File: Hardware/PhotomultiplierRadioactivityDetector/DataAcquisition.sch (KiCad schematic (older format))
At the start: 27 parts, among them Q1 2N7002, Q2 Q_NJFET_DGS, Q7 Q_NJFET_DGS, U1 TL074, U3 TL074

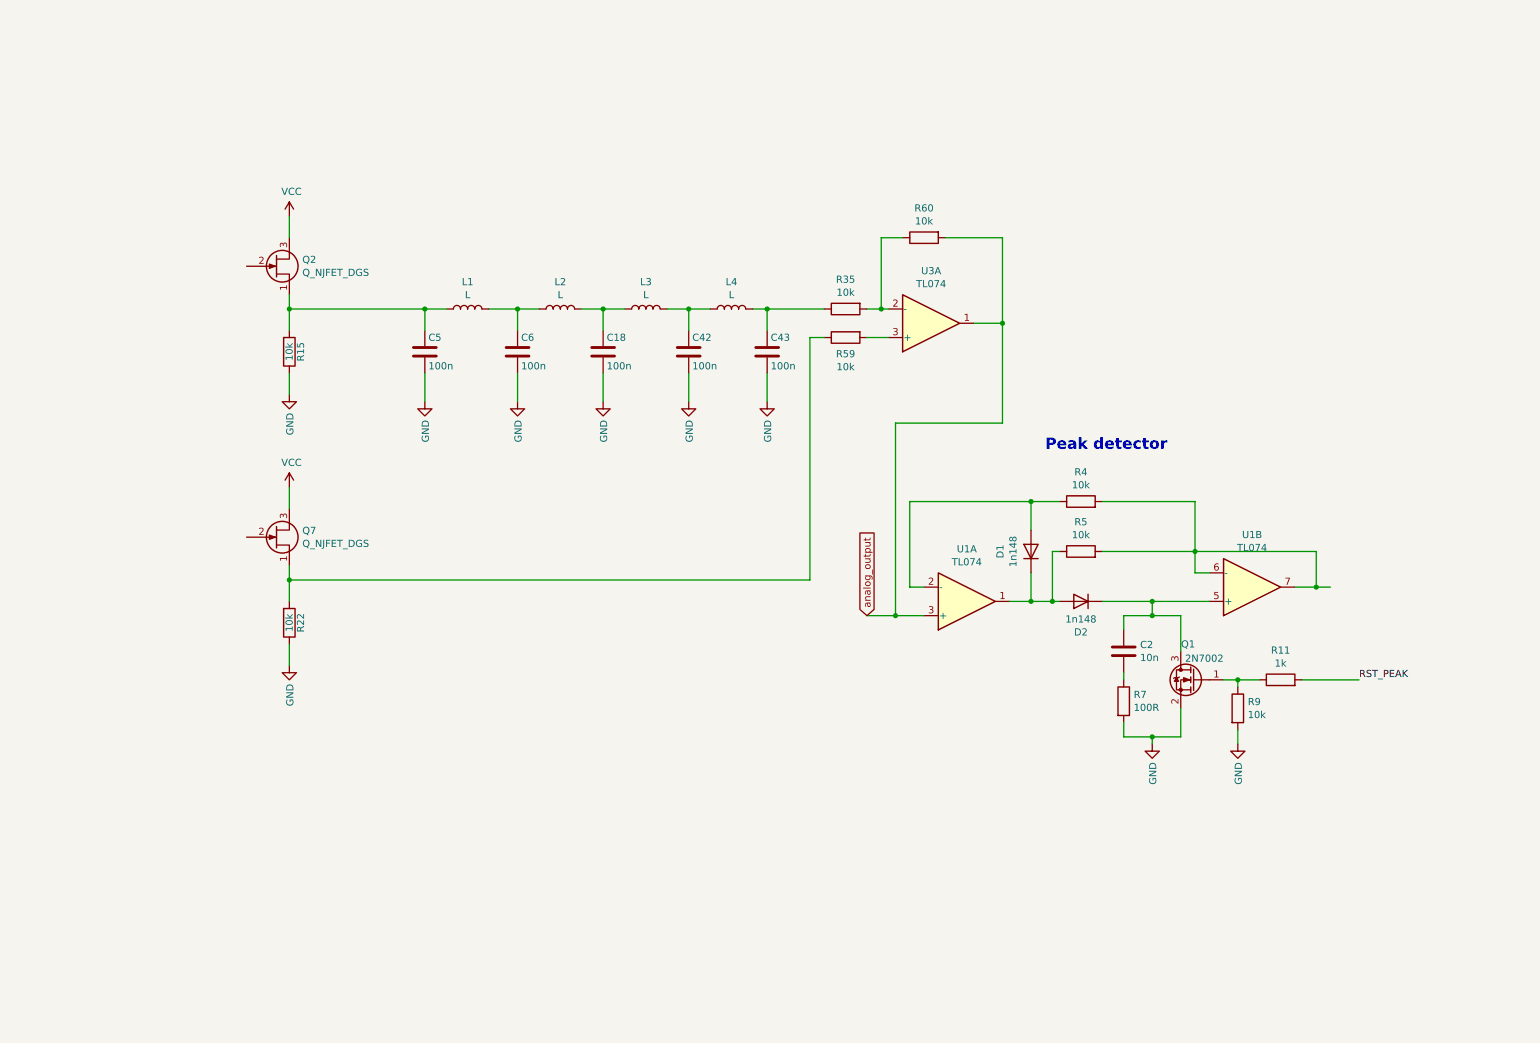
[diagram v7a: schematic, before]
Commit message: align to ltspice simulation
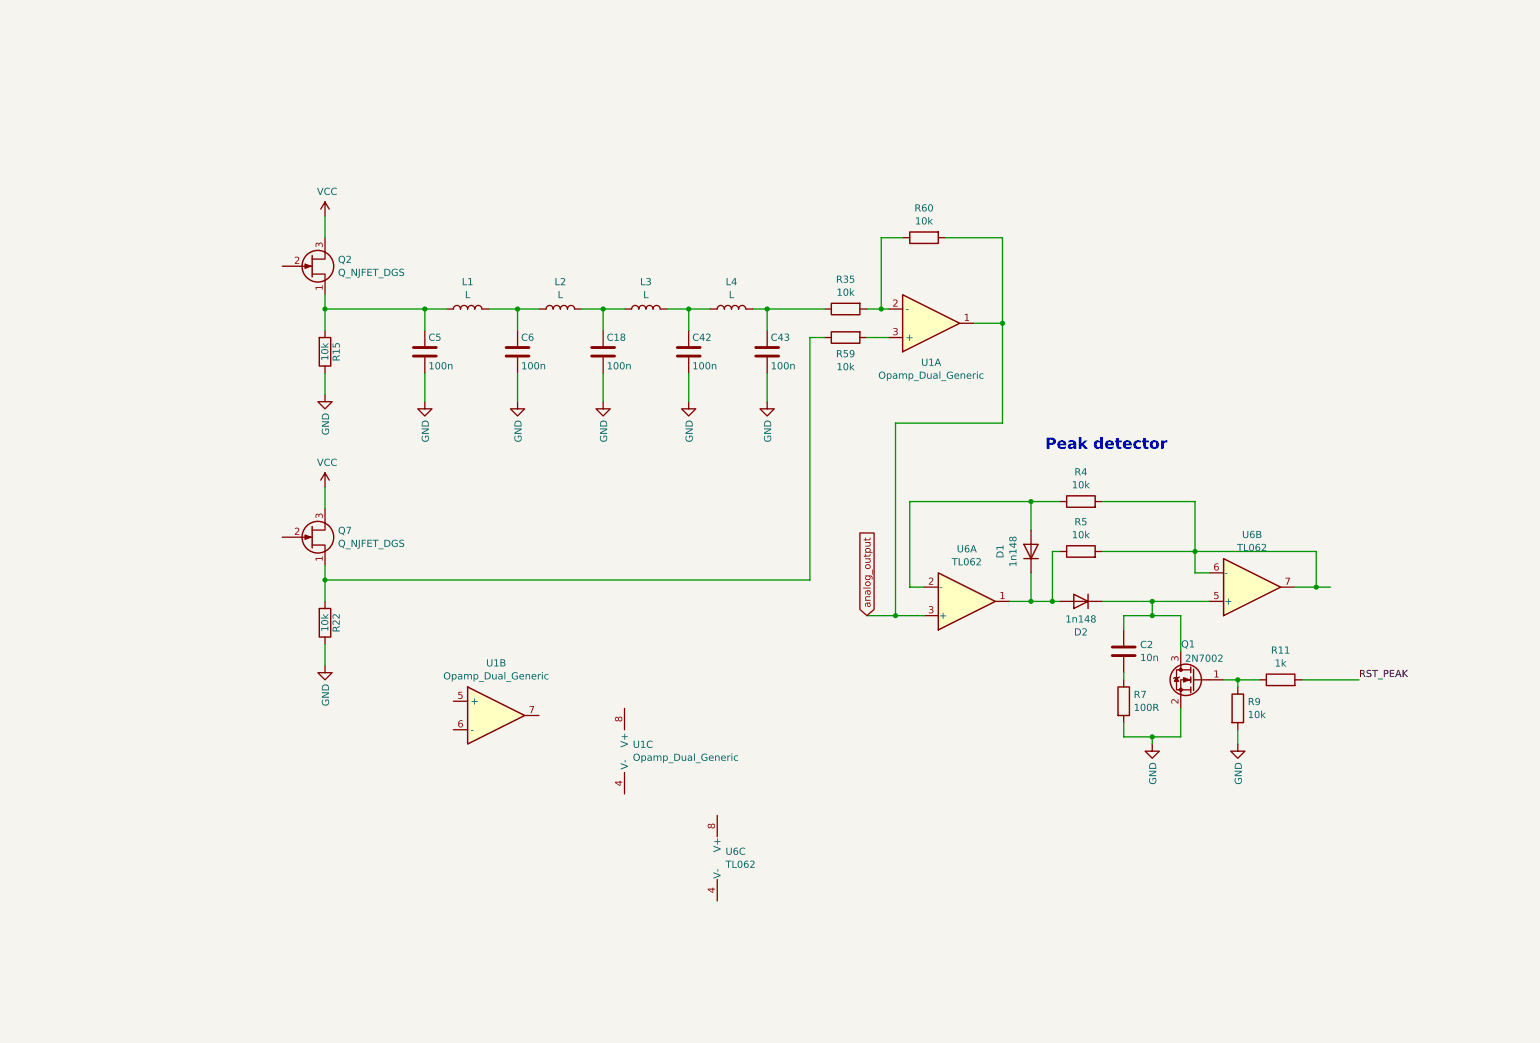
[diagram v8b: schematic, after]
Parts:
- removed U1, U3: TL074, Package_SO:SOIC-14_3.9x8.7mm_P1.27mm, symbol Amplifier_Operational:TL074
- added U1: Opamp_Dual_Generic, Package_SO:MSOP-8-1EP_3x3mm_P0.65mm_EP1.68x1.88mm, symbol Device:Opamp_Dual_Generic
- added U6: TL062, Package_SO:SO-8_5.3x6.2mm_P1.27mm, symbol Amplifier_Operational:TL062
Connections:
- net analog_output: now also U1.1, U6.3 (+)
- net at D1.1 (K), D2.2 (A), R5.1: now also U6.1
- net at D1.2 (A), R4.1: now also U6.2 (-)
- net at C2.2, D2.1 (K), Q1.3 (D): now also U6.5 (+)
- net at R4.2, R5.2: now also U6.6 (-), U6.7
- net at R35.2, R60.1: now also U1.2 (-)
- net at R59.2: now also U1.3 (+)
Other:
- moved on the sheet: Q2, Q7, R15, R22
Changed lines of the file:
@@
 Wire Wire Line
 	9200 5250 9350 5250
-$Comp
-L Amplifier_Operational:TL074 U1
-U 1 1 5ED99C75
-P 7300 4700
-F 0 "U1" H 7300 4333 50  0000 C CNN
-F 1 "TL074" H 7300 4424 50  0000 C CNN
-F 2 "Package_SO:SOIC-14_3.9x8.7mm_P1.27mm" H 7250 4800 50  0001 C CNN
-F 3 "http://www.ti.com/lit/ds/symlink/tl071.pdf" H 7350 4900 50  0001 C CNN
-	1    7300 4700
-	1    0    0    1
-$EndComp
-$Comp
-L Amplifier_Operational:TL074 U1
-U 2 1 5ED9B4E9
-P 9300 4600
-F 0 "U1" H 9300 4233 50  0000 C CNN
-F 1 "TL074" H 9300 4324 50  0000 C CNN
-F 2 "Package_SO:SOIC-14_3.9x8.7mm_P1.27mm" H 9250 4700 50  0001 C CNN
-F 3 "http://www.ti.com/lit/ds/symlink/tl071.pdf" H 9350 4800 50  0001 C CNN
-	2    9300 4600
-	1    0    0    1
-$EndComp
 Text Notes 7850 3650 0    79   ~ 16
 Peak detector
@@
 L Device:R R?
 U 1 1 5F1121BE
-P 2550 2950
+P 2800 2950
 AR Path="/5EFA52FA/5F1121BE" Ref="R?"  Part="1"
 AR Path="/5EE9D63B/5F1121BE" Ref="R?"  Part="1"
 AR Path="/5EE61922/5F1121BE" Ref="R?"  Part="1"
 AR Path="/5EDA53F3/5F1121BE" Ref="R15"  Part="1"
-F 0 "R15" V 2630 2950 50  0000 C CNN
-F 1 "10k" V 2550 2950 50  0000 C CNN
-F 2 "Resistor_SMD:R_0805_2012Metric_Pad1.15x1.40mm_HandSolder" V 2480 2950 50  0001 C CNN
-F 3 "" H 2550 2950 50  0001 C CNN
-	1    2550 2950
+F 0 "R15" V 2880 2950 50  0000 C CNN
+F 1 "10k" V 2800 2950 50  0000 C CNN
+F 2 "Resistor_SMD:R_0805_2012Metric_Pad1.15x1.40mm_HandSolder" V 2730 2950 50  0001 C CNN
+F 3 "" H 2800 2950 50  0001 C CNN
+	1    2800 2950
 	1    0    0    1
 $EndComp
@@
 L Device:Q_NJFET_DGS Q?
 U 1 1 5F1121C4
-P 2450 2350
+P 2700 2350
 AR Path="/5EE9D63B/5F1121C4" Ref="Q?"  Part="1"
 AR Path="/5EE61922/5F1121C4" Ref="Q?"  Part="1"
 AR Path="/5EDA53F3/5F1121C4" Ref="Q2"  Part="1"
-F 0 "Q2" H 2641 2304 50  0000 L CNN
-F 1 "Q_NJFET_DGS" H 2641 2395 50  0000 L CNN
-F 2 "Package_TO_SOT_SMD:SC-59" H 2650 2450 50  0001 C CNN
-F 3 "~" H 2450 2350 50  0001 C CNN
-	1    2450 2350
-	1    0    0    1
-$EndComp
-Wire Wire Line
-	2550 2650 2550 2550
-Wire Wire Line
-	2550 2800 2550 2650
-Connection ~ 2550 2650
-Wire Wire Line
-	2550 3250 2550 3100
-Wire Wire Line
-	2550 2650 3500 2650
+F 0 "Q2" H 2891 2304 50  0000 L CNN
+F 1 "Q_NJFET_DGS" H 2891 2395 50  0000 L CNN
+F 2 "Package_TO_SOT_SMD:SC-59" H 2900 2450 50  0001 C CNN
+F 3 "~" H 2700 2350 50  0001 C CNN
+	1    2700 2350
+	1    0    0    1
+$EndComp
+Wire Wire Line
+	2800 2650 2800 2550
+Wire Wire Line
+	2800 2800 2800 2650
+Connection ~ 2800 2650
+Wire Wire Line
+	2800 3250 2800 3100
+Wire Wire Line
+	2800 2650 3500 2650
 $Comp
 L Device:L L1
@@
 L power:GND #PWR014
 U 1 1 5F11A2FD
-P 2550 3250
-F 0 "#PWR014" H 2550 3000 50  0001 C CNN
-F 1 "GND" V 2555 3122 50  0000 R CNN
-F 2 "" H 2550 3250 50  0001 C CNN
-F 3 "" H 2550 3250 50  0001 C CNN
-	1    2550 3250
+P 2800 3250
+F 0 "#PWR014" H 2800 3000 50  0001 C CNN
+F 1 "GND" V 2805 3122 50  0000 R CNN
+F 2 "" H 2800 3250 50  0001 C CNN
+F 3 "" H 2800 3250 50  0001 C CNN
+	1    2800 3250
 	1    0    0    -1
 $EndComp
@@
 L power:VCC #PWR012
 U 1 1 5F11E793
-P 2550 2000
-F 0 "#PWR012" H 2550 1850 50  0001 C CNN
-F 1 "VCC" H 2565 2173 50  0000 C CNN
-F 2 "" H 2550 2000 50  0001 C CNN
-F 3 "" H 2550 2000 50  0001 C CNN
-	1    2550 2000
-	1    0    0    -1
-$EndComp
-Wire Wire Line
-	2550 2150 2550 2000
+P 2800 2000
+F 0 "#PWR012" H 2800 1850 50  0001 C CNN
+F 1 "VCC" H 2815 2173 50  0000 C CNN
+F 2 "" H 2800 2000 50  0001 C CNN
+F 3 "" H 2800 2000 50  0001 C CNN
+	1    2800 2000
+	1    0    0    -1
+$EndComp
+Wire Wire Line
+	2800 2150 2800 2000
 $Comp
 L power:GND #PWR024
@@
 Wire Wire Line
 	5350 3300 5350 3100
-$Comp
-L Amplifier_Operational:TL074 U3
-U 1 1 5F12C94C
-P 7050 2750
-F 0 "U3" H 7050 2383 50  0000 C CNN
-F 1 "TL074" H 7050 2474 50  0000 C CNN
-F 2 "Package_SO:SOIC-14_3.9x8.7mm_P1.27mm" H 7000 2850 50  0001 C CNN
-F 3 "http://www.ti.com/lit/ds/symlink/tl071.pdf" H 7100 2950 50  0001 C CNN
-	1    7050 2750
-	1    0    0    1
-$EndComp
 $Comp
 L Device:R R?
@@
 L Device:R R?
 U 1 1 5F13AA9D
-P 2550 4850
+P 2800 4850
 AR Path="/5EFA52FA/5F13AA9D" Ref="R?"  Part="1"
 AR Path="/5EE9D63B/5F13AA9D" Ref="R?"  Part="1"
 AR Path="/5EE61922/5F13AA9D" Ref="R?"  Part="1"
 AR Path="/5EDA53F3/5F13AA9D" Ref="R22"  Part="1"
-F 0 "R22" V 2630 4850 50  0000 C CNN
-F 1 "10k" V 2550 4850 50  0000 C CNN
-F 2 "Resistor_SMD:R_0805_2012Metric_Pad1.15x1.40mm_HandSolder" V 2480 4850 50  0001 C CNN
-F 3 "" H 2550 4850 50  0001 C CNN
-	1    2550 4850
+F 0 "R22" V 2880 4850 50  0000 C CNN
+F 1 "10k" V 2800 4850 50  0000 C CNN
+F 2 "Resistor_SMD:R_0805_2012Metric_Pad1.15x1.40mm_HandSolder" V 2730 4850 50  0001 C CNN
+F 3 "" H 2800 4850 50  0001 C CNN
+	1    2800 4850
 	1    0    0    1
 $EndComp
@@
 L Device:Q_NJFET_DGS Q?
 U 1 1 5F13AAA3
-P 2450 4250
+P 2700 4250
 AR Path="/5EE9D63B/5F13AAA3" Ref="Q?"  Part="1"
 AR Path="/5EE61922/5F13AAA3" Ref="Q?"  Part="1"
 AR Path="/5EDA53F3/5F13AAA3" Ref="Q7"  Part="1"
-F 0 "Q7" H 2641 4204 50  0000 L CNN
-F 1 "Q_NJFET_DGS" H 2641 4295 50  0000 L CNN
-F 2 "Package_TO_SOT_SMD:SC-59" H 2650 4350 50  0001 C CNN
-F 3 "~" H 2450 4250 50  0001 C CNN
-	1    2450 4250
-	1    0    0    1
-$EndComp
-Wire Wire Line
-	2550 4550 2550 4450
-Wire Wire Line
-	2550 4700 2550 4550
-Connection ~ 2550 4550
-Wire Wire Line
-	2550 5150 2550 5000
+F 0 "Q7" H 2891 4204 50  0000 L CNN
+F 1 "Q_NJFET_DGS" H 2891 4295 50  0000 L CNN
+F 2 "Package_TO_SOT_SMD:SC-59" H 2900 4350 50  0001 C CNN
+F 3 "~" H 2700 4250 50  0001 C CNN
+	1    2700 4250
+	1    0    0    1
+$EndComp
+Wire Wire Line
+	2800 4550 2800 4450
+Wire Wire Line
+	2800 4700 2800 4550
+Connection ~ 2800 4550
+Wire Wire Line
+	2800 5150 2800 5000
 $Comp
 L power:GND #PWR016
 U 1 1 5F13AAAE
-P 2550 5150
-F 0 "#PWR016" H 2550 4900 50  0001 C CNN
-F 1 "GND" V 2555 5022 50  0000 R CNN
-F 2 "" H 2550 5150 50  0001 C CNN
-F 3 "" H 2550 5150 50  0001 C CNN
-	1    2550 5150
+P 2800 5150
+F 0 "#PWR016" H 2800 4900 50  0001 C CNN
+F 1 "GND" V 2805 5022 50  0000 R CNN
+F 2 "" H 2800 5150 50  0001 C CNN
+F 3 "" H 2800 5150 50  0001 C CNN
+	1    2800 5150
 	1    0    0    -1
 $EndComp
@@
 L power:VCC #PWR015
 U 1 1 5F13AAB4
-P 2550 3900
-F 0 "#PWR015" H 2550 3750 50  0001 C CNN
-F 1 "VCC" H 2565 4073 50  0000 C CNN
-F 2 "" H 2550 3900 50  0001 C CNN
-F 3 "" H 2550 3900 50  0001 C CNN
-	1    2550 3900
-	1    0    0    -1
-$EndComp
-Wire Wire Line
-	2550 4050 2550 3900
-Wire Wire Line
-	2550 4550 6200 4550
+P 2800 3900
+F 0 "#PWR015" H 2800 3750 50  0001 C CNN
+F 1 "VCC" H 2815 4073 50  0000 C CNN
+F 2 "" H 2800 3900 50  0001 C CNN
+F 3 "" H 2800 3900 50  0001 C CNN
+	1    2800 3900
+	1    0    0    -1
+$EndComp
+Wire Wire Line
+	2800 4050 2800 3900
+Wire Wire Line
+	2800 4550 6200 4550
 Wire Wire Line
 	6600 2650 6700 2650
@@
 Wire Wire Line
 	6800 4800 6600 4800
+$Comp
+L Amplifier_Operational:TL062 U6
+U 1 1 5F1FAFCA
+P 7300 4700
+F 0 "U6" H 7300 4333 50  0000 C CNN
+F 1 "TL062" H 7300 4424 50  0000 C CNN
+F 2 "Package_SO:SO-8_5.3x6.2mm_P1.27mm" H 7300 4700 50  0001 C CNN
+F 3 "http://www.ti.com/lit/ds/symlink/tl061.pdf" H 7300 4700 50  0001 C CNN
+	1    7300 4700
+	1    0    0    1
+$EndComp
+$Comp
+L Amplifier_Operational:TL062 U6
+U 2 1 5F1FD903
+P 9300 4600
+F 0 "U6" H 9300 4233 50  0000 C CNN
+F 1 "TL062" H 9300 4324 50  0000 C CNN
+F 2 "Package_SO:SO-8_5.3x6.2mm_P1.27mm" H 9300 4600 50  0001 C CNN
+F 3 "http://www.ti.com/lit/ds/symlink/tl061.pdf" H 9300 4600 50  0001 C CNN
+	2    9300 4600
+	1    0    0    1
+$EndComp
+$Comp
+L Amplifier_Operational:TL062 U6
+U 3 1 5F1FF002
+P 5650 6500
+F 0 "U6" H 5608 6546 50  0000 L CNN
+F 1 "TL062" H 5608 6455 50  0000 L CNN
+F 2 "Package_SO:SO-8_5.3x6.2mm_P1.27mm" H 5650 6500 50  0001 C CNN
+F 3 "http://www.ti.com/lit/ds/symlink/tl061.pdf" H 5650 6500 50  0001 C CNN
+	3    5650 6500
+	1    0    0    -1
+$EndComp
+$Comp
+L Device:Opamp_Dual_Generic U1
+U 1 1 5F21CB18
+P 7050 2750
+F 0 "U1" H 7050 3025 50  0000 C CNN
+F 1 "Opamp_Dual_Generic" H 7050 3116 50  0000 C CNN
+F 2 "Package_SO:MSOP-8-1EP_3x3mm_P0.65mm_EP1.68x1.88mm" H 7050 2750 50  0001 C CNN
+F 3 "~" H 7050 2750 50  0001 C CNN
+	1    7050 2750
+	1    0    0    1
+$EndComp
+$Comp
+L Device:Opamp_Dual_Generic U1
+U 2 1 5F21D4DD
+P 4000 5500
+F 0 "U1" H 4000 5867 50  0000 C CNN
+F 1 "Opamp_Dual_Generic" H 4000 5776 50  0000 C CNN
+F 2 "Package_SO:MSOP-8-1EP_3x3mm_P0.65mm_EP1.68x1.88mm" H 4000 5500 50  0001 C CNN
+F 3 "~" H 4000 5500 50  0001 C CNN
+	2    4000 5500
+	1    0    0    -1
+$EndComp
+$Comp
+L Device:Opamp_Dual_Generic U1
+U 3 1 5F21DFF6
+P 5000 5750
+F 0 "U1" H 4958 5796 50  0000 L CNN
+F 1 "Opamp_Dual_Generic" H 4958 5705 50  0000 L CNN
+F 2 "Package_SO:MSOP-8-1EP_3x3mm_P0.65mm_EP1.68x1.88mm" H 5000 5750 50  0001 C CNN
+F 3 "~" H 5000 5750 50  0001 C CNN
+	3    5000 5750
+	1    0    0    -1
+$EndComp
 $EndSCHEMATC
